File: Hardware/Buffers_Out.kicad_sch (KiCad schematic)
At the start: 29 parts, among them U4 MCP6002-xSN, X1 PEDAL_COMBO_TOP

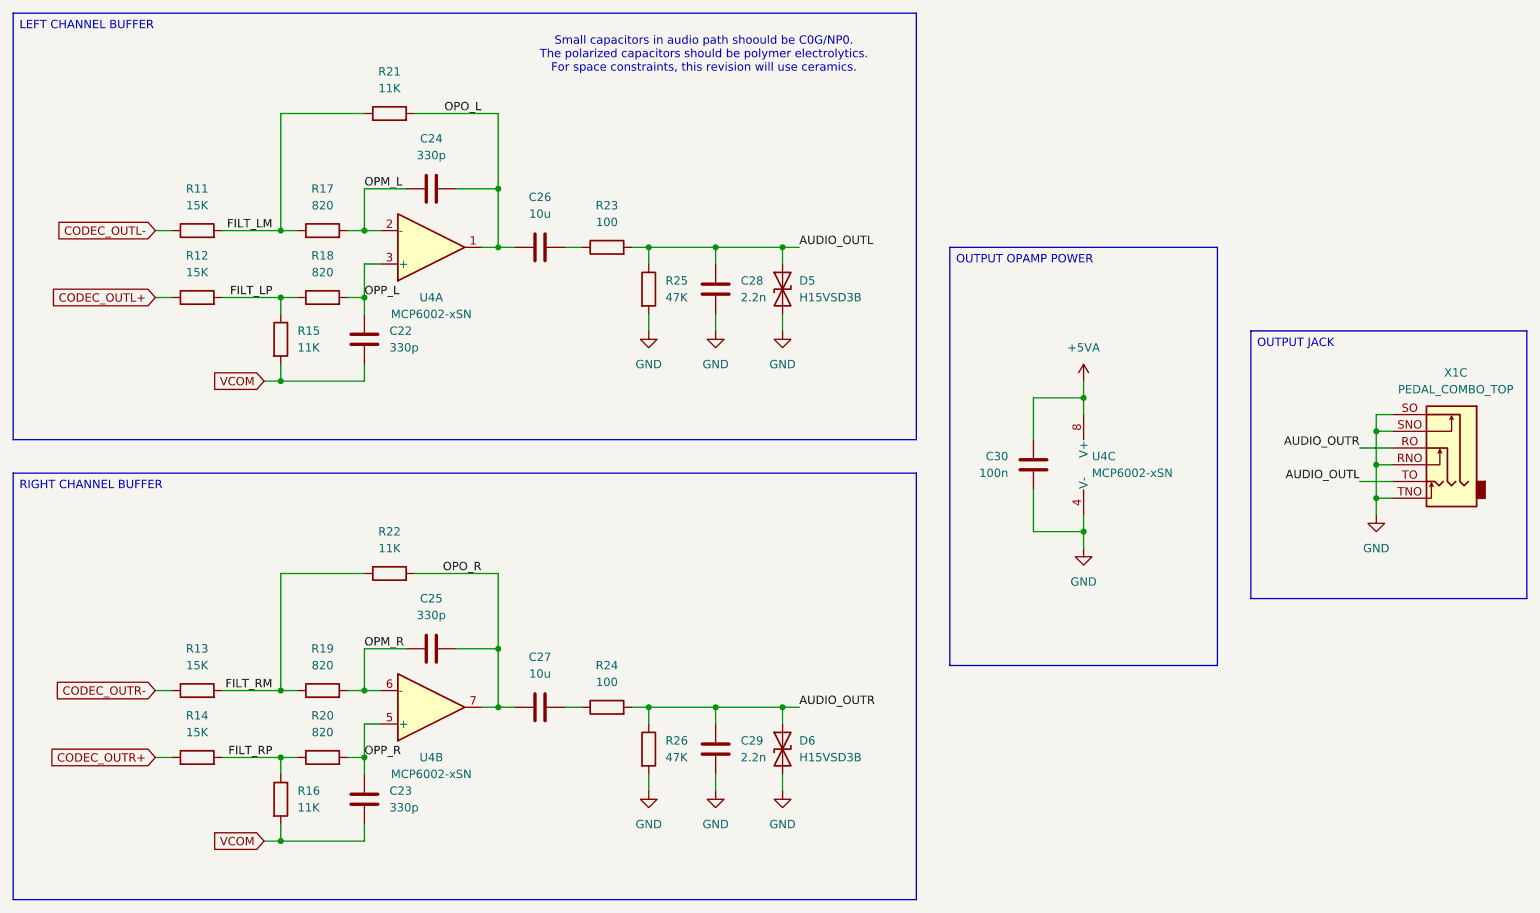
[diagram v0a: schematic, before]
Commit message: Layout review
Updated the LDO layout to include a series resistor for stability.
Updated all build files.
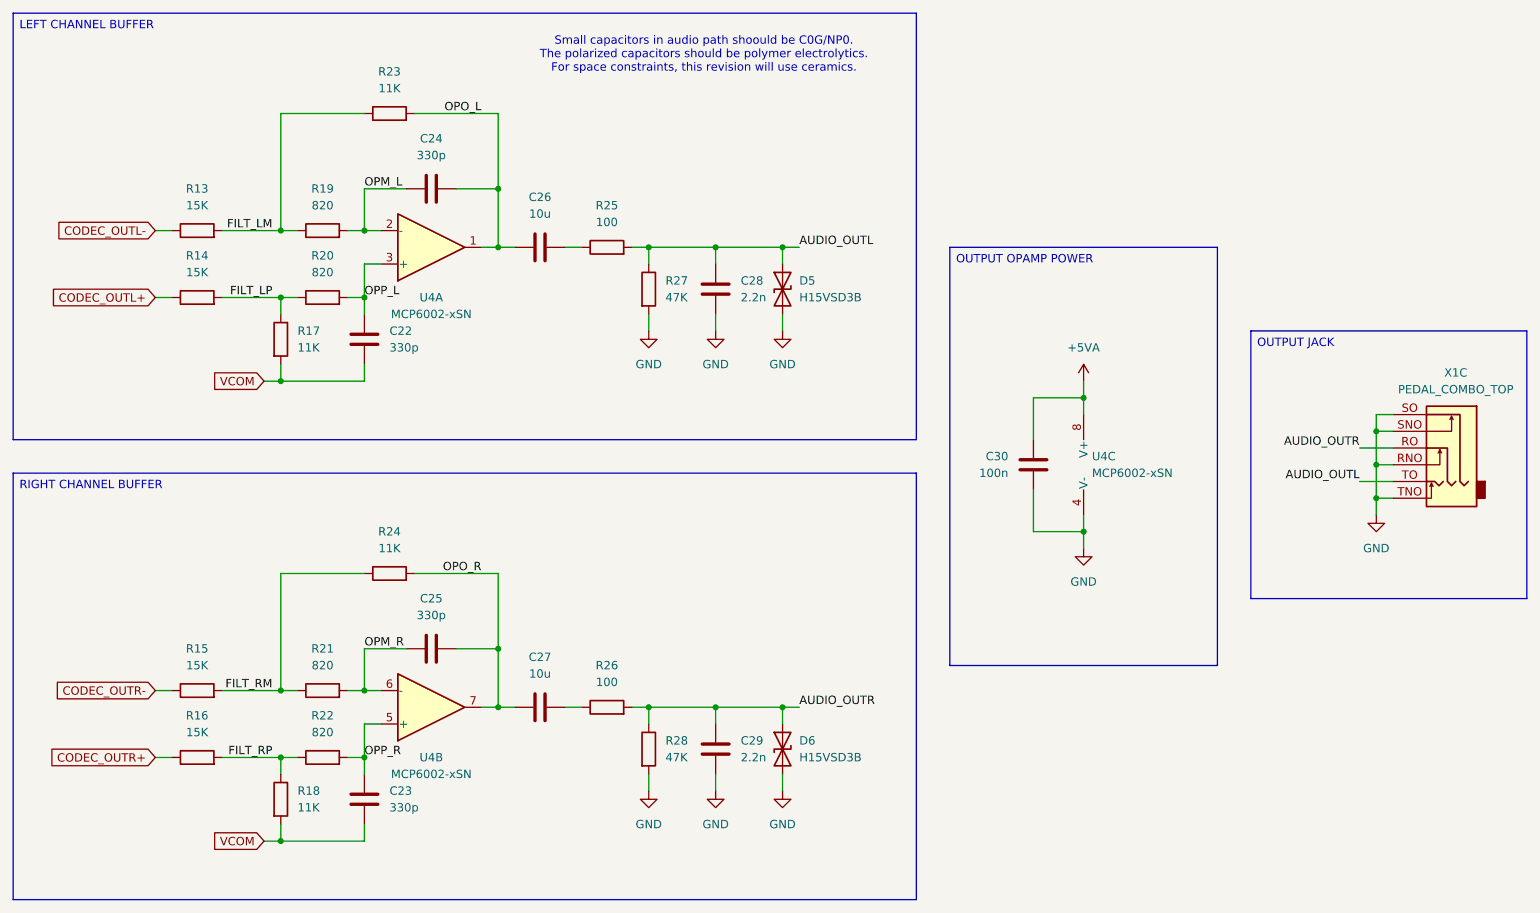
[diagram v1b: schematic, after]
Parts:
- renumbered R11 to R13, R12 to R14, R13 to R15, R14 to R16, R15 to R17, R16 to R18, R17 to R19, R18 to R20, R19 to R21, R20 to R22, R21 to R23, R22 to R24, R23 to R25, R24 to R26, R25 to R27, R26 to R28
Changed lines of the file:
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@@
 		(in_pos_files yes)
 		(dnp no)
-		(property "Reference" "R16"
+		(property "Reference" "R18"
 			(at 83.82 139.6999 0)
 			(show_name no)
@@
 			(project "PicoFX"
 				(path "/4cbf131b-42e8-4a05-beea-68c6d66cdb1a/f30b69e3-f4a5-44b3-bff9-cd489323ac3e"
-					(reference "R16")
+					(reference "R18")
 					(unit 1)
 				)
@@
 		(dnp no)
 		(fields_autoplaced yes)
-		(property "Reference" "R14"
+		(property "Reference" "R16"
 			(at 68.58 128.27 90)
 			(show_name no)
@@
 			(project "PicoFX"
 				(path "/4cbf131b-42e8-4a05-beea-68c6d66cdb1a/f30b69e3-f4a5-44b3-bff9-cd489323ac3e"
-					(reference "R14")
+					(reference "R16")
 					(unit 1)
 				)
@@
 		(dnp no)
 		(fields_autoplaced yes)
-		(property "Reference" "R26"
+		(property "Reference" "R28"
 			(at 139.7 132.0799 0)
 			(show_name no)
@@
 			(project "PicoFX"
 				(path "/4cbf131b-42e8-4a05-beea-68c6d66cdb1a/f30b69e3-f4a5-44b3-bff9-cd489323ac3e"
-					(reference "R26")
+					(reference "R28")
 					(unit 1)
 				)
@@
 		(dnp no)
 		(fields_autoplaced yes)
-		(property "Reference" "R21"
+		(property "Reference" "R23"
 			(at 97.79 30.48 90)
 			(show_name no)
@@
 			(project "PicoFX"
 				(path "/4cbf131b-42e8-4a05-beea-68c6d66cdb1a/f30b69e3-f4a5-44b3-bff9-cd489323ac3e"
-					(reference "R21")
+					(reference "R23")
 					(unit 1)
 				)
@@
 		(dnp no)
 		(fields_autoplaced yes)
-		(property "Reference" "R12"
+		(property "Reference" "R14"
 			(at 68.58 58.42 90)
 			(show_name no)
@@
 			(project "PicoFX"
 				(path "/4cbf131b-42e8-4a05-beea-68c6d66cdb1a/f30b69e3-f4a5-44b3-bff9-cd489323ac3e"
-					(reference "R12")
+					(reference "R14")
 					(unit 1)
 				)
@@
 		(in_pos_files yes)
 		(dnp no)
-		(property "Reference" "R15"
+		(property "Reference" "R17"
 			(at 83.82 69.8499 0)
 			(show_name no)
@@
 			(project "PicoFX"
 				(path "/4cbf131b-42e8-4a05-beea-68c6d66cdb1a/f30b69e3-f4a5-44b3-bff9-cd489323ac3e"
-					(reference "R15")
+					(reference "R17")
 					(unit 1)
 				)
@@
 		(dnp no)
 		(fields_autoplaced yes)
-		(property "Reference" "R18"
+		(property "Reference" "R20"
 			(at 87.63 58.42 90)
 			(show_name no)
@@
 			(project "PicoFX"
 				(path "/4cbf131b-42e8-4a05-beea-68c6d66cdb1a/f30b69e3-f4a5-44b3-bff9-cd489323ac3e"
-					(reference "R18")
+					(reference "R20")
 					(unit 1)
 				)
@@
 		(dnp no)
 		(fields_autoplaced yes)
-		(property "Reference" "R20"
+		(property "Reference" "R22"
 			(at 87.63 128.27 90)
 			(show_name no)
@@
 			(project "PicoFX"
 				(path "/4cbf131b-42e8-4a05-beea-68c6d66cdb1a/f30b69e3-f4a5-44b3-bff9-cd489323ac3e"
-					(reference "R20")
+					(reference "R22")
 					(unit 1)
 				)
@@
 		(dnp no)
 		(fields_autoplaced yes)
-		(property "Reference" "R25"
+		(property "Reference" "R27"
 			(at 139.7 62.2299 0)
 			(show_name no)
@@
 			(project "PicoFX"
 				(path "/4cbf131b-42e8-4a05-beea-68c6d66cdb1a/f30b69e3-f4a5-44b3-bff9-cd489323ac3e"
-					(reference "R25")
+					(reference "R27")
 					(unit 1)
 				)
@@
 		(dnp no)
 		(fields_autoplaced yes)
-		(property "Reference" "R17"
+		(property "Reference" "R19"
 			(at 87.63 48.26 90)
 			(show_name no)
@@
 			(project "PicoFX"
 				(path "/4cbf131b-42e8-4a05-beea-68c6d66cdb1a/f30b69e3-f4a5-44b3-bff9-cd489323ac3e"
-					(reference "R17")
+					(reference "R19")
 					(unit 1)
 				)
@@
 		(dnp no)
 		(fields_autoplaced yes)
-		(property "Reference" "R22"
+		(property "Reference" "R24"
 			(at 97.79 100.33 90)
 			(show_name no)
@@
 			(project "PicoFX"
 				(path "/4cbf131b-42e8-4a05-beea-68c6d66cdb1a/f30b69e3-f4a5-44b3-bff9-cd489323ac3e"
-					(reference "R22")
+					(reference "R24")
 					(unit 1)
 				)
@@
 		(dnp no)
 		(fields_autoplaced yes)
-		(property "Reference" "R13"
+		(property "Reference" "R15"
 			(at 68.58 118.11 90)
 			(show_name no)
@@
 			(project "PicoFX"
 				(path "/4cbf131b-42e8-4a05-beea-68c6d66cdb1a/f30b69e3-f4a5-44b3-bff9-cd489323ac3e"
-					(reference "R13")
+					(reference "R15")
 					(unit 1)
 				)
@@
 		(dnp no)
 		(fields_autoplaced yes)
-		(property "Reference" "R24"
+		(property "Reference" "R26"
 			(at 130.81 120.65 90)
 			(show_name no)
@@
 			(project "PicoFX"
 				(path "/4cbf131b-42e8-4a05-beea-68c6d66cdb1a/f30b69e3-f4a5-44b3-bff9-cd489323ac3e"
-					(reference "R24")
+					(reference "R26")
 					(unit 1)
 				)
@@
 		(dnp no)
 		(fields_autoplaced yes)
-		(property "Reference" "R23"
+		(property "Reference" "R25"
 			(at 130.81 50.8 90)
 			(show_name no)
@@
 			(project "PicoFX"
 				(path "/4cbf131b-42e8-4a05-beea-68c6d66cdb1a/f30b69e3-f4a5-44b3-bff9-cd489323ac3e"
-					(reference "R23")
+					(reference "R25")
 					(unit 1)
 				)
@@
 		(dnp no)
 		(fields_autoplaced yes)
-		(property "Reference" "R19"
+		(property "Reference" "R21"
 			(at 87.63 118.11 90)
 			(show_name no)
@@
 			(project "PicoFX"
 				(path "/4cbf131b-42e8-4a05-beea-68c6d66cdb1a/f30b69e3-f4a5-44b3-bff9-cd489323ac3e"
-					(reference "R19")
+					(reference "R21")
 					(unit 1)
 				)
@@
 		(dnp no)
 		(fields_autoplaced yes)
-		(property "Reference" "R11"
+		(property "Reference" "R13"
 			(at 68.58 48.26 90)
 			(show_name no)
@@
 			(project "PicoFX"
 				(path "/4cbf131b-42e8-4a05-beea-68c6d66cdb1a/f30b69e3-f4a5-44b3-bff9-cd489323ac3e"
-					(reference "R11")
+					(reference "R13")
 					(unit 1)
 				)

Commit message: Output files
Updated the board silkscreen.
Upddated the output files.
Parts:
- C22, C23, C24, C25: JLCPCB Part (none) -> C1664; Manufacturer Part (none) -> CL10C331JB8NNNC
- C26, C27: JLCPCB Part (none) -> C15850; Manufacturer Part (none) -> CL21A106KAYNNNE
- C28, C29: JLCPCB Part (none) -> C28260; Manufacturer Part (none) -> CL21C222JBFNNNE
- C30: JLCPCB Part (none) -> C14663; Manufacturer Part (none) -> CC0603KRX7R9BB104
- D5, D6: JLCPCB Part (none) -> C20615814; Manufacturer Part (none) -> H15VSD3B
- R13, R14, R15, R16: JLCPCB Part (none) -> C22809; Manufacturer Part (none) -> 0603WAF1502T5E
- R17, R18, R23, R24: JLCPCB Part (none) -> C25950; Manufacturer Part (none) -> 0603WAF1102T5E
- R19, R20, R21, R22: JLCPCB Part (none) -> C23253; Manufacturer Part (none) -> 0603WAF8200T5E
- R25, R26: JLCPCB Part (none) -> C22775; Manufacturer Part (none) -> 0603WAF1000T5E
- R27, R28: JLCPCB Part (none) -> C25819; Manufacturer Part (none) -> 0603WAF4702T5E
- U4: JLCPCB Part (none) -> C7377; Manufacturer Part (none) -> MCP6002T-I/SN
- X1: now left out of the parts list

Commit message: Assembly review
Performed a full review of the schematic and layout.
Minor changes to the schematic and layout.
Updated output files.
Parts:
- X1: JLCPCB Part (none) -> -; Manufacturer Part (none) -> -
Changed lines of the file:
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@@
+			)
+		)
+		(property "JLCPCB Part" "-"
+			(at 259.08 88.9 0)
+			(hide yes)
+			(show_name no)
+			(do_not_autoplace no)
+			(effects
+				(font
+					(size 1.27 1.27)
+				)
+			)
+		)
+		(property "Manufacturer Part" "-"
+			(at 259.08 88.9 0)
+			(hide yes)
+			(show_name no)
+			(do_not_autoplace no)
+			(effects
+				(font
+					(size 1.27 1.27)
+				)
 			)
 		)
